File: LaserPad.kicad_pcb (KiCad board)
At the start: 2 copper layers, 72 parts, among them J1 USB_C_Receptacle_USB2.0_16P, SW1 RST, SW2 RST, U1 STM32F072CBTx, U2 74AHCT1G125, U3 PRTR5V0U2X, U4 USBLC6-2SC6, U5 XC6206PxxxMR-Regulator_Linear

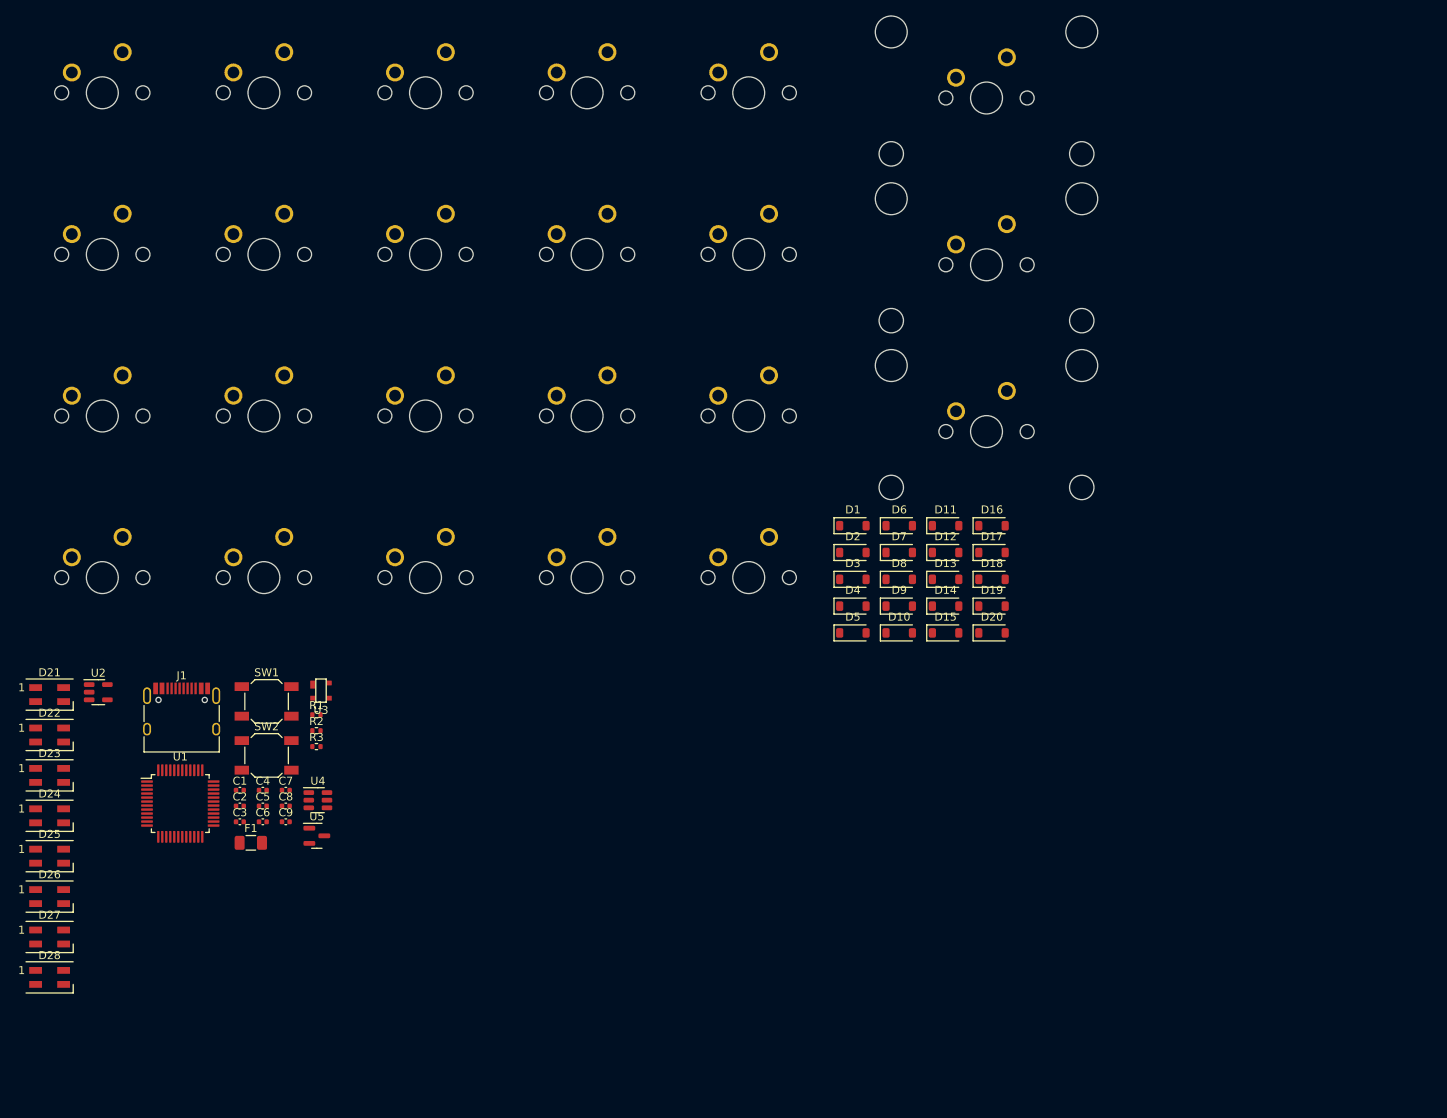
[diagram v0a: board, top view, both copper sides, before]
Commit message: Placed Components and in the process of routing
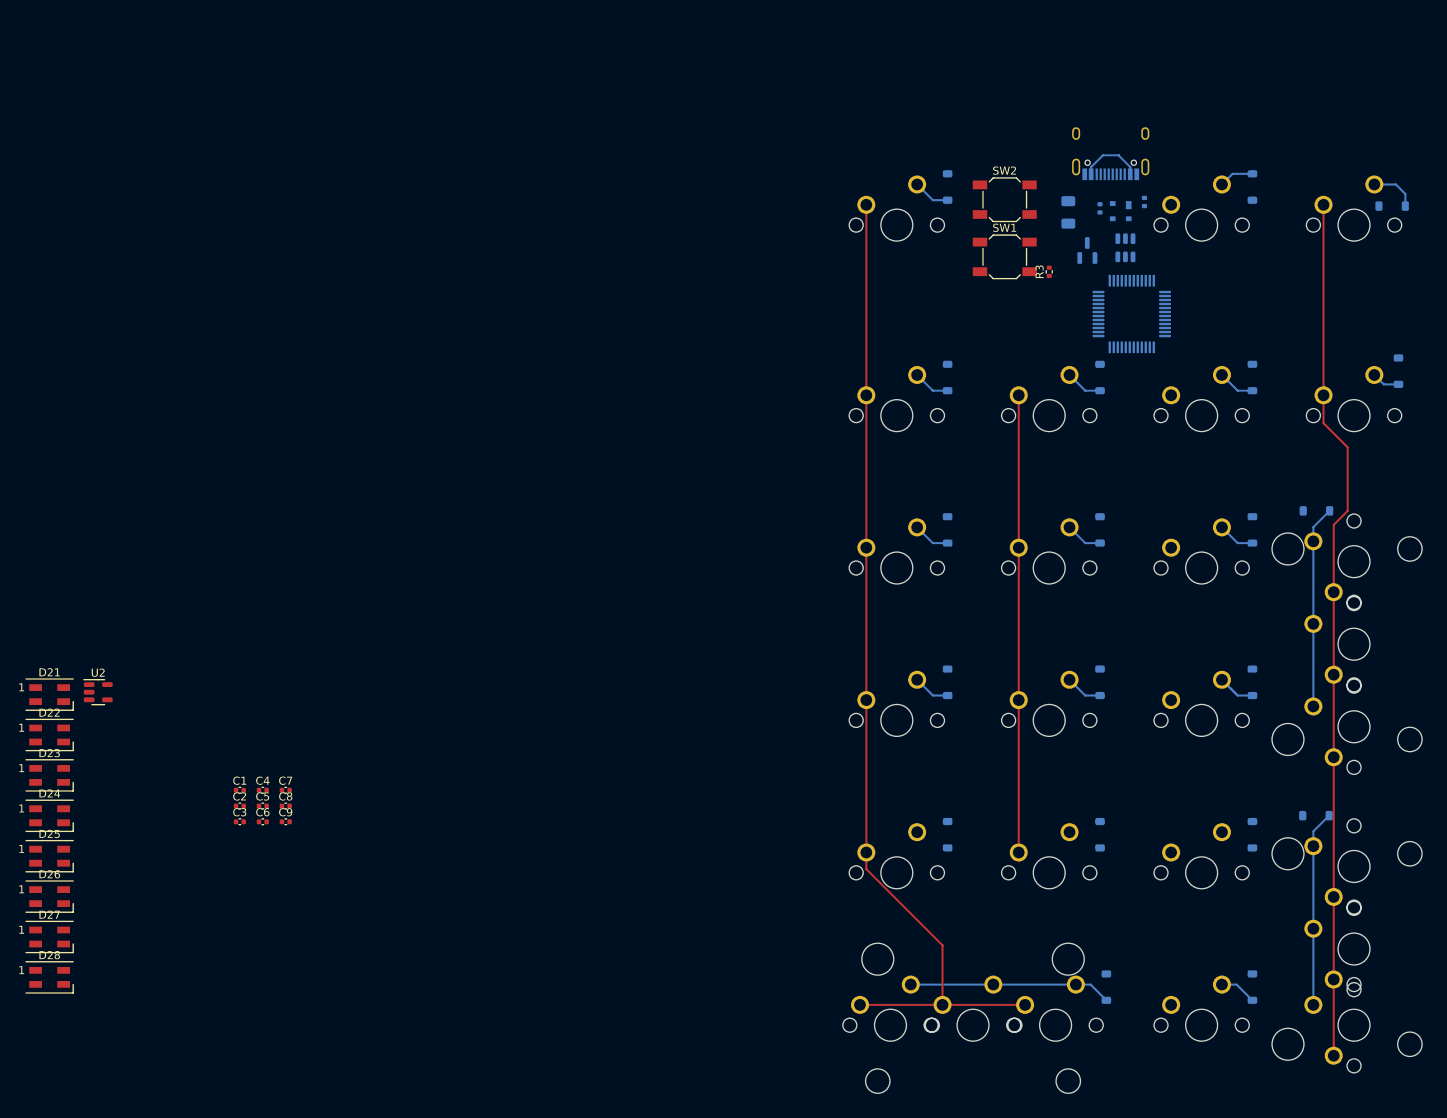
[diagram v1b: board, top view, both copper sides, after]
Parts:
- removed D8: SOD-123, Diode_SMD:D_SOD-123
- added D29: SOD-123, Diode_SMD:D_SOD-123, B.Cu at (165.1, 133.3)
- added MX24: MX-NoLED, MX_Only:MXOnly-1U-NoLED, F.Cu at (158.8, 138.1)
- added MX25: MX-NoLED, MX_Only:MXOnly-1U-NoLED, F.Cu at (177.8, 138.1)
- added MX26: MX-NoLED, MX_Only:MXOnly-1U-NoLED, F.Cu at (140.5, 138.1)
- D1, D10, D11, D12, D13, D14, D15, D16, D17, D18, D19, D2, D20, D3, D4, D5, D6, D7, D9, F1, J1, R1, R2, U1, U3, U4, U5: moved to B.Cu
- moved MX4 162.5 mm to (177.8, 38.1)
- moved MX3 139.5 mm to (158.8, 38.1)
- moved MX2 137.8 mm to (119.9, 138.1)
- moved MX8 137.8 mm to (177.8, 61.9)
- moved J1 136.8 mm to (147.4, 27.7)
- moved U1 133.8 mm to (150.0, 49.2), turned to -90 degrees
- moved F1 129.0 mm to (142.1, 36.5), turned to -90 degrees
- moved R2 122.8 mm to (151.6, 35.2), turned to -90 degrees
- moved U4 122.3 mm to (149.2, 40.9), turned to -90 degrees
- moved U5 120.9 mm to (144.5, 41.3), turned to 90 degrees
- moved MX7 117.2 mm to (158.8, 61.9)
- moved R1 116.6 mm to (146.1, 36.0), turned to -90 degrees
- moved U3 116.6 mm to (148.6, 36.4), turned to 180 degrees
- moved MX12 116.1 mm to (177.8, 80.2), turned to 90 degrees
- moved MX21 115.9 mm to (130.2, 138.1)
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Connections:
- D18 pad 1: ROW0 -> ROW5
- MX16 pad 2: Net-(D8-A) -> Net-(D1-A)
- MX2 pad 1: COL1 -> COL0
- MX21 pad 2: Net-(D9-A) -> Net-(D18-A)
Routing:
- net COL0: track 0.00 -> 124.6 mm
- net COL3: track 0.00 -> 108.3 mm
- net COL1: track 0.00 -> 58.3 mm
- net Net-(D1-A): track 0.00 -> 25.3 mm
- net Net-(D18-A): track 0.00 -> 25.3 mm
- net Net-(D12-A): track 0.00 -> 24.5 mm
- net +5V: track 0.00 -> 7.97 mm
- net Net-(D7-A): track 0.00 -> 7.32 mm
- net Net-(D20-A): track 0.00 -> 5.88 mm
- net Net-(D6-A): track 0.00 -> 4.62 mm
- net Net-(D5-A): track 0.00 -> 4.62 mm
- net Net-(D4-A): track 0.00 -> 4.62 mm
- net Net-(D3-A): track 0.00 -> 4.62 mm
- net Net-(D29-A): track 0.00 -> 4.62 mm
- net Net-(D2-A): track 0.00 -> 4.62 mm
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
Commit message: Almost done placing components into PCB
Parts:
- C2, C4, C5, C7, C8, C9, D21, D22, D23, D24, D25, D26, D27, D28: moved to B.Cu
- moved D28 175.8 mm to (184.9, 88.1), turned to -90 degrees
- moved D27 170.9 mm to (184.9, 112.1), turned to -90 degrees
- moved D26 145.9 mm to (158.8, 145.3), turned to 180 degrees
- moved D21 137.6 mm to (135.6, 30.9), turned to 180 degrees
- moved C3 136.9 mm to (159.9, 49.2)
- moved C5 130.1 mm to (152.4, 42.9), turned to 180 degrees
- moved C4 129.1 mm to (157.2, 51.6), turned to 90 degrees
- moved C8 123.9 mm to (144.5, 37.8), turned to -90 degrees
- moved D25 123.5 mm to (134.9, 145.3), turned to 180 degrees
- moved C2 123.2 mm to (148.7, 55.6)
- moved C9 119.5 mm to (142.1, 44.0), turned to 90 degrees
- moved C6 116.6 mm to (139.7, 50.0)
- moved C7 116.4 mm to (142.9, 46.8), turned to -90 degrees
- moved D22 112.0 mm to (114.4, 50.6), turned to -90 degrees
- moved D23 101.0 mm to (114.3, 89.7), turned to -90 degrees
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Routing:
- net COL2: track 0.00 -> 100.0 mm
- net +5V: track 7.97 -> 0.00 mm
- net Net-(D9-A): track 0.00 -> 4.62 mm
- net Net-(D11-A): track 0.00 -> 4.62 mm
- net Net-(D10-A): track 0.00 -> 4.62 mm
- net Net-(D14-A): track 4.62 -> 2.94 mm

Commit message: many changes
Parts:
- C1, U2: moved to B.Cu
- moved U2 114.4 mm to (125.4, 50.0), turned to 180 degrees
- moved C1 113.2 mm to (128.6, 40.2), turned to 90 degrees
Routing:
- net COL0: track 124.6 -> 121.9 mm

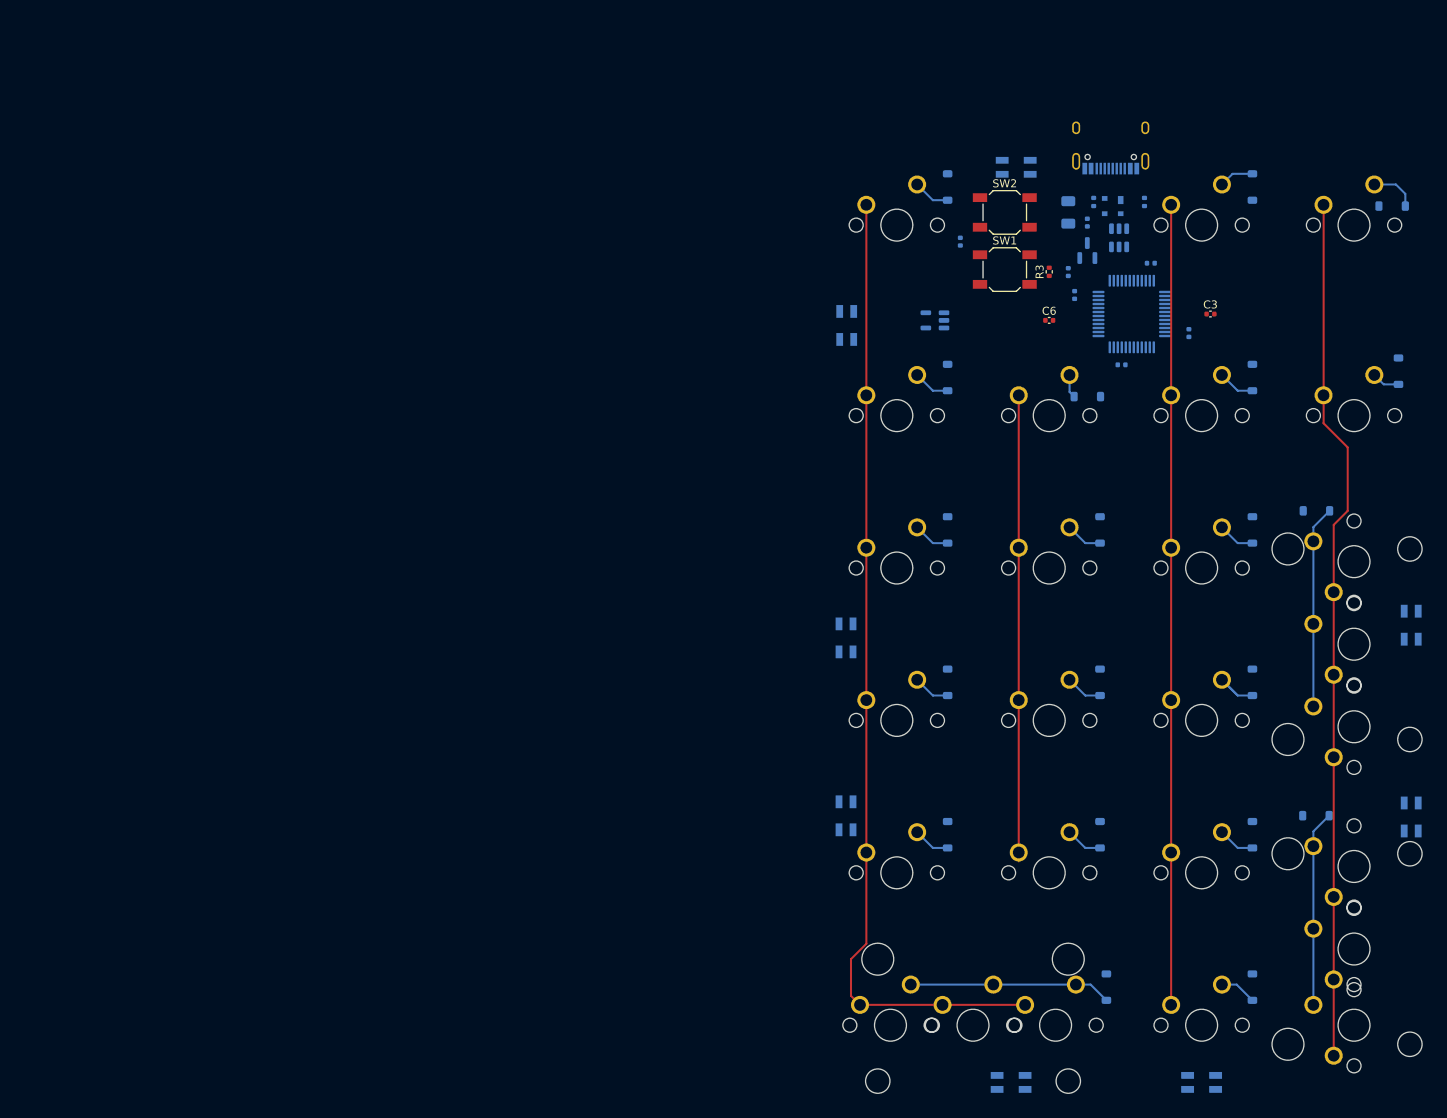
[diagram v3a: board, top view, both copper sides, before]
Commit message: Changed around a couple of objects for new reset circuit
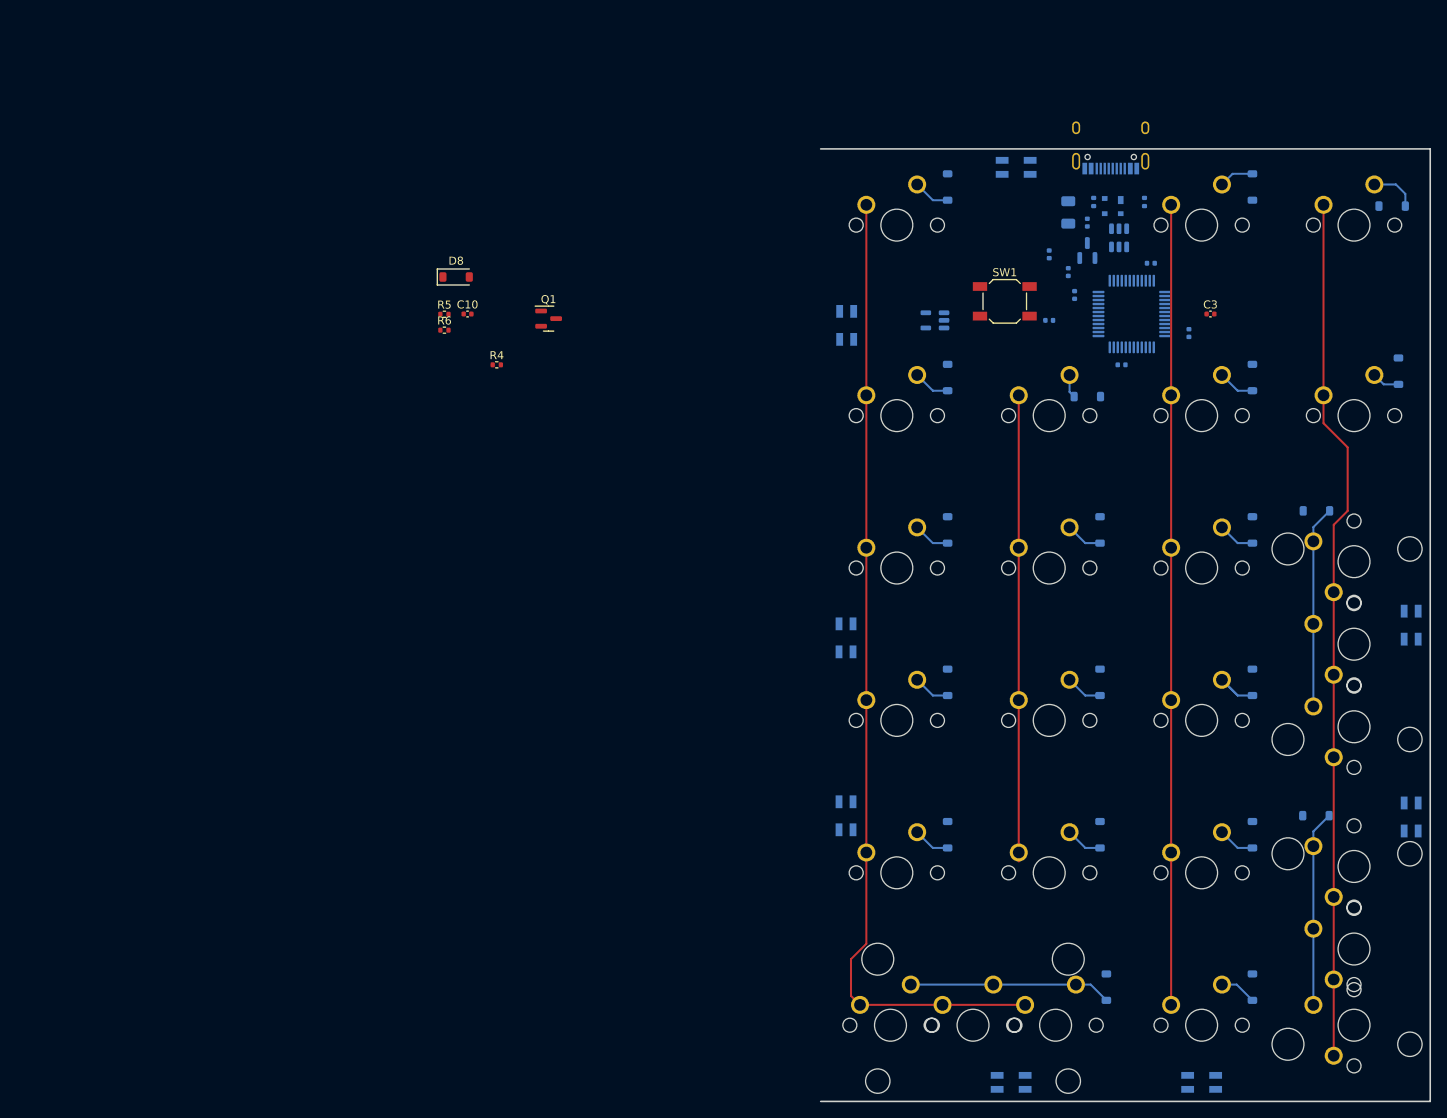
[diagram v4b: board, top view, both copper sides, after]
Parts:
- removed R3: 10k, Resistor_SMD:R_0402_1005Metric
- removed SW2: RST, Button_Switch_SMD:SW_SPST_SKQG_WithoutStem
- added C10: 10uF, Capacitor_SMD:C_0402_1005Metric, F.Cu at (67.0, 49.2)
- added D8: SOD-123, Diode_SMD:D_SOD-123, F.Cu at (65.6, 44.6)
- added Q1: DTC123J, Package_TO_SOT_SMD:SOT-23, F.Cu at (77.1, 49.8)
- added R4: 100, Resistor_SMD:R_0402_1005Metric, F.Cu at (70.6, 55.6)
- added R5: 300k, Resistor_SMD:R_0402_1005Metric, F.Cu at (64.1, 49.2)
- added R6: 1M, Resistor_SMD:R_0402_1005Metric, F.Cu at (64.1, 51.2)
- C6: moved to B.Cu
- moved C1 11.2 mm to (139.7, 41.8)
- moved SW1 3.97 mm to (134.1, 47.6)
- turned C6 to 180 degrees
- turned U1 to 90 degrees
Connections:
- SW1 pad 2: BOOT0 -> Net-(D8-A)
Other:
- board outline added: 76.2 x 119.1 mm

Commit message: Changed reset circuit yet again :/
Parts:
- added Q2: 2N7002, Package_TO_SOT_SMD:SOT-23, B.Cu at (151.8, 67.5)
- added R10: 10k, Resistor_SMD:R_0402_1005Metric, F.Cu at (77.2, 54.9)
- added R3: 10k, Resistor_SMD:R_0402_1005Metric, F.Cu at (77.2, 41.0)
- added R7: 1k, Resistor_SMD:R_0402_1005Metric, F.Cu at (77.2, 48.9)
- added R8: 10k, Resistor_SMD:R_0402_1005Metric, B.Cu at (157.4, 49.2)
- added R9: 100k, Resistor_SMD:R_0402_1005Metric, F.Cu at (77.2, 52.9)
- C3, D8, SW1: moved to B.Cu
- Q1: value DTC123J -> 2N7002; moved to B.Cu
- moved D8 85.6 mm to (147.6, 69.1), turned to 90 degrees
- moved Q1 74.0 mm to (150.2, 61.9), turned to 180 degrees
- moved C10 18.4 mm to (85.0, 53.0)
- moved C1 18.0 mm to (151.3, 55.6), turned to 180 degrees
- moved R4 14.2 mm to (77.2, 43.0)
- moved R5 13.8 mm to (77.2, 45.0)
- moved R6 13.8 mm to (77.2, 47.0)
- moved SW1 6.40 mm to (133.3, 54.0), turned to 180 degrees
- moved C3 0.96 mm to (160.8, 49.2), turned to 180 degrees
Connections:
- C1 pad 1: GND -> NRST
- C1 pad 2: NRST -> GND
- Q1 pad 1: Net-(D8-A) -> Net-(Q1-G)
